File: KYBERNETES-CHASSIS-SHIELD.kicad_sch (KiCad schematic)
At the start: 42 parts, among them J1 ESC, J10 Fan, J2 Radio, J3 Encoder, J4 I2C, J5 Bumper, J6 Servo 1, J7 Servo 2, J8 Servo Regulator 1, J9 Servo Regulator 2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

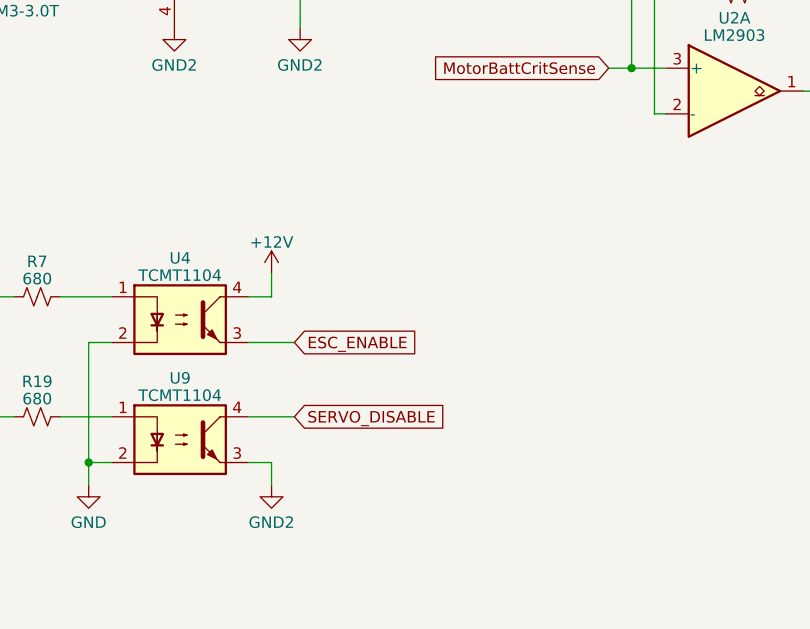
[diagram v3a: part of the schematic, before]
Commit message: add a mosfet after the esc enable opto to as it is not just an enable line as previously thought. needs more current than opto can provide.
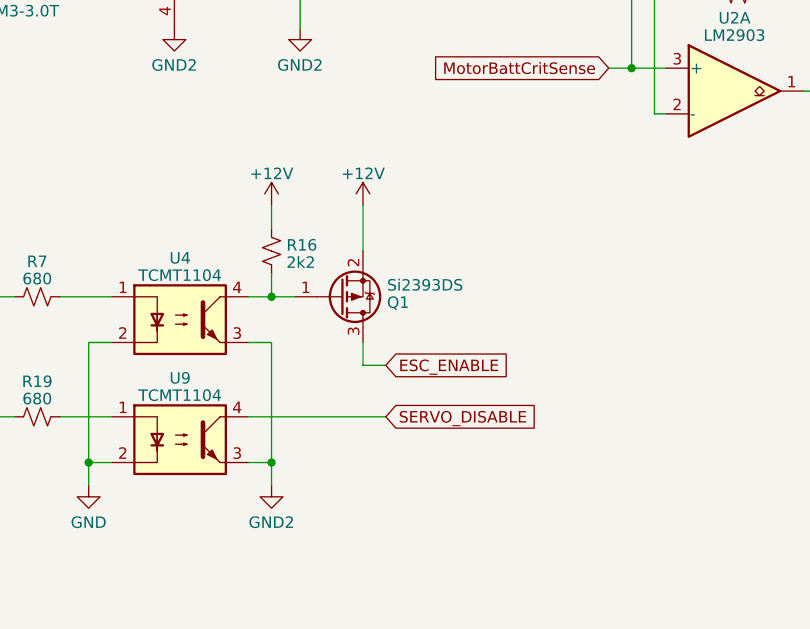
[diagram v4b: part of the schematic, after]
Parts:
- added Q1: Si2393DS, Package_TO_SOT_SMD:SOT-23, symbol Mosfets:Si2393DS
- added R16: 2k2, Resistor_SMD:R_0603_1608Metric_Pad0.98x0.95mm_HandSolder, symbol Device:R_Small_US
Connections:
- net +12V: now also Q1.2 (S), R16.1; no longer U4.4
- net ESC_ENABLE: now also Q1.3 (D); no longer U4.3
- net GND2: now also U4.3
- new net: Q1.1 (G), R16.2, U4.4
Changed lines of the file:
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@@
   (junction (at 116.84 250.19) (diameter 0) (color 0 0 0 0)
   )
+  (junction (at 137.795 175.895) (diameter 0) (color 0 0 0 0)
+  )
   (junction (at 117.475 59.055) (diameter 0) (color 0 0 0 0)
   )
@@
   (junction (at 145.415 236.855) (diameter 0) (color 0 0 0 0)
   )
+  (junction (at 137.795 194.31) (diameter 0) (color 0 0 0 0)
+  )
   (junction (at 297.18 64.135) (diameter 0) (color 0 0 0 0)
   )
@@
     (stroke (width 0) (type default))
   )
+  (wire (pts (xy 137.795 180.975) (xy 135.255 180.975))
+    (stroke (width 0) (type default))
+  )
   (wire (pts (xy 164.465 51.435) (xy 169.545 51.435))
     (stroke (width 0) (type default))
@@
     (stroke (width 0) (type default))
   )
+  (wire (pts (xy 147.955 183.515) (xy 150.495 183.515))
+    (stroke (width 0) (type default))
+  )
   (wire (pts (xy 40.005 136.525) (xy 40.005 137.795))
     (stroke (width 0) (type default))
@@
     (stroke (width 0) (type default))
   )
-  (wire (pts (xy 135.255 175.895) (xy 137.795 175.895))
-    (stroke (width 0) (type default))
-  )
   (wire (pts (xy 167.005 59.055) (xy 169.545 59.055))
     (stroke (width 0) (type default))
@@
     (stroke (width 0) (type default))
   )
-  (wire (pts (xy 137.795 173.355) (xy 137.795 175.895))
-    (stroke (width 0) (type default))
-  )
   (wire (pts (xy 145.415 236.855) (xy 155.575 236.855))
     (stroke (width 0) (type default))
@@
     (stroke (width 0) (type default))
   )
+  (wire (pts (xy 137.795 175.895) (xy 140.335 175.895))
+    (stroke (width 0) (type default))
+  )
   (wire (pts (xy 153.035 257.81) (xy 153.035 260.35))
     (stroke (width 0) (type default))
@@
     (stroke (width 0) (type default))
   )
-  (wire (pts (xy 135.255 189.23) (xy 140.335 189.23))
+  (wire (pts (xy 135.255 189.23) (xy 150.495 189.23))
     (stroke (width 0) (type default))
   )
@@
     (stroke (width 0) (type default))
   )
+  (wire (pts (xy 135.255 175.895) (xy 137.795 175.895))
+    (stroke (width 0) (type default))
+  )
   (wire (pts (xy 158.75 67.945) (xy 158.75 69.215))
     (stroke (width 0) (type default))
@@
     (stroke (width 0) (type default))
   )
+  (wire (pts (xy 147.955 165.735) (xy 147.955 170.815))
+    (stroke (width 0) (type default))
+  )
   (wire (pts (xy 117.475 59.055) (xy 117.475 69.215))
     (stroke (width 0) (type default))
@@
     (stroke (width 0) (type default))
   )
-  (wire (pts (xy 135.255 180.975) (xy 140.335 180.975))
-    (stroke (width 0) (type default))
-  )
   (wire (pts (xy 346.71 191.135) (xy 349.25 191.135))
     (stroke (width 0) (type default))
@@
     (stroke (width 0) (type default))
   )
+  (wire (pts (xy 137.795 165.735) (xy 137.795 168.275))
+    (stroke (width 0) (type default))
+  )
+  (wire (pts (xy 137.795 194.31) (xy 137.795 180.975))
+    (stroke (width 0) (type default))
+  )
+  (wire (pts (xy 147.955 180.975) (xy 147.955 183.515))
+    (stroke (width 0) (type default))
+  )
   (wire (pts (xy 342.9 147.955) (xy 346.71 147.955))
     (stroke (width 0) (type default))
@@
     (stroke (width 0) (type default))
   )
+  (wire (pts (xy 137.795 173.355) (xy 137.795 175.895))
+    (stroke (width 0) (type default))
+  )
   (wire (pts (xy 313.69 196.215) (xy 316.23 196.215))
     (stroke (width 0) (type default))
@@
     )
   )
-  (global_label "ESC_ENABLE" (shape input) (at 140.335 180.975 0) (fields_autoplaced)
+  (global_label "ESC_ENABLE" (shape input) (at 150.495 183.515 0) (fields_autoplaced)
     (effects (font (size 1.27 1.27)) (justify left))
-    (property "Intersheetrefs" "${INTERSHEET_REFS}" (at 154.8521 180.975 0)
+    (property "Intersheetrefs" "${INTERSHEET_REFS}" (at 165.0121 183.515 0)
       (effects (font (size 1.27 1.27)) (justify left) hide)
     )
@@
     )
   )
-  (global_label "SERVO_DISABLE" (shape input) (at 140.335 189.23 0) (fields_autoplaced)
+  (global_label "SERVO_DISABLE" (shape input) (at 150.495 189.23 0) (fields_autoplaced)
     (effects (font (size 1.27 1.27)) (justify left))
-    (property "Intersheetrefs" "${INTERSHEET_REFS}" (at 157.876 189.23 0)
+    (property "Intersheetrefs" "${INTERSHEET_REFS}" (at 168.036 189.23 0)
       (effects (font (size 1.27 1.27)) (justify left) hide)
     )
@@
     )
   )
+  (symbol (lib_id "Device:R_Small_US") (at 137.795 170.815 0) (unit 1)
+    (in_bom yes) (on_board yes) (dnp no) (fields_autoplaced)
+    (property "Reference" "R16" (at 139.446 170.1713 0)
+      (effects (font (size 1.27 1.27)) (justify left))
+    )
+    (property "Value" "2k2" (at 139.446 172.0923 0)
+      (effects (font (size 1.27 1.27)) (justify left))
+    )
+    (property "Footprint" "Resistor_SMD:R_0603_1608Metric_Pad0.98x0.95mm_HandSolder" (at 137.795 170.815 0)
+      (effects (font (size 1.27 1.27)) hide)
+    )
+    (property "Datasheet" "~" (at 137.795 170.815 0)
+      (effects (font (size 1.27 1.27)) hide)
+    )
+    (pin "1")
+    (pin "2")
+    (instances
+      (project "KYBERNETES-CHASSIS-SHIELD"
+        (path "/35172950-fd0b-46e4-875b-9133eac965de"
+          (reference "R16") (unit 1)
+        )
+      )
+      (project "KYBERNETES-CHASSIS-PD"
+        (path "/b9e34260-dded-46d4-944b-b6d38e23aefa"
+          (reference "R20") (unit 1)
+        )
+      )
+    )
+  )
   (symbol (lib_id "power:GND2") (at 117.475 69.215 0) (unit 1)
     (in_bom yes) (on_board yes) (dnp no) (fields_autoplaced)
@@
     )
   )
+  (symbol (lib_id "Mosfets:Si2393DS") (at 145.415 175.895 0) (mirror x) (unit 1)
+    (in_bom yes) (on_board yes) (dnp no)
+    (property "Reference" "Q1" (at 150.622 176.5387 0)
+      (effects (font (size 1.27 1.27)) (justify left))
+    )
+    (property "Value" "Si2393DS" (at 150.622 174.6177 0)
+      (effects (font (size 1.27 1.27)) (justify left))
+    )
+    (property "Footprint" "Package_TO_SOT_SMD:SOT-23" (at 150.495 173.99 0)
+      (effects (font (size 1.27 1.27) italic) (justify left) hide)
+    )
+    (property "Datasheet" "https://www.vishay.com/docs/70132/si2393ds.pdf" (at 145.415 175.895 0)
+      (effects (font (size 1.27 1.27)) (justify left) hide)
+    )
+    (pin "1")
+    (pin "2")
+    (pin "3")
+    (instances
+      (project "KYBERNETES-CHASSIS-SHIELD"
+        (path "/35172950-fd0b-46e4-875b-9133eac965de"
+          (reference "Q1") (unit 1)
+        )
+      )
+    )
+  )
   (symbol (lib_id "power:+12V") (at 40.005 128.905 0) (unit 1)
     (in_bom yes) (on_board yes) (dnp no) (fields_autoplaced)
@@
     )
   )
-  (symbol (lib_id "power:+12V") (at 137.795 173.355 0) (unit 1)
+  (symbol (lib_id "power:+12V") (at 137.795 165.735 0) (unit 1)
     (in_bom yes) (on_board yes) (dnp no) (fields_autoplaced)
-    (property "Reference" "#PWR029" (at 137.795 177.165 0)
+    (property "Reference" "#PWR029" (at 137.795 169.545 0)
       (effects (font (size 1.27 1.27)) hide)
     )
-    (property "Value" "+12V" (at 137.795 169.8531 0)
+    (property "Value" "+12V" (at 137.795 162.2331 0)
       (effects (font (size 1.27 1.27)))
     )
-    (property "Footprint" "" (at 137.795 173.355 0)
+    (property "Footprint" "" (at 137.795 165.735 0)
       (effects (font (size 1.27 1.27)) hide)
     )
-    (property "Datasheet" "" (at 137.795 173.355 0)
+    (property "Datasheet" "" (at 137.795 165.735 0)
       (effects (font (size 1.27 1.27)) hide)
     )
@@
         )
       )
+    )
+  )
+  (symbol (lib_id "power:+12V") (at 147.955 165.735 0) (unit 1)
+    (in_bom yes) (on_board yes) (dnp no) (fields_autoplaced)
+    (property "Reference" "#PWR052" (at 147.955 169.545 0)
+      (effects (font (size 1.27 1.27)) hide)
+    )
+    (property "Value" "+12V" (at 147.955 162.2331 0)
+      (effects (font (size 1.27 1.27)))
+    )
+    (property "Footprint" "" (at 147.955 165.735 0)
+      (effects (font (size 1.27 1.27)) hide)
+    )
+    (property "Datasheet" "" (at 147.955 165.735 0)
+      (effects (font (size 1.27 1.27)) hide)
+    )
+    (pin "1")
+    (instances
+      (project "KYBERNETES-CHASSIS-SHIELD"
+        (path "/35172950-fd0b-46e4-875b-9133eac965de"
+          (reference "#PWR052") (unit 1)
+        )
+      )

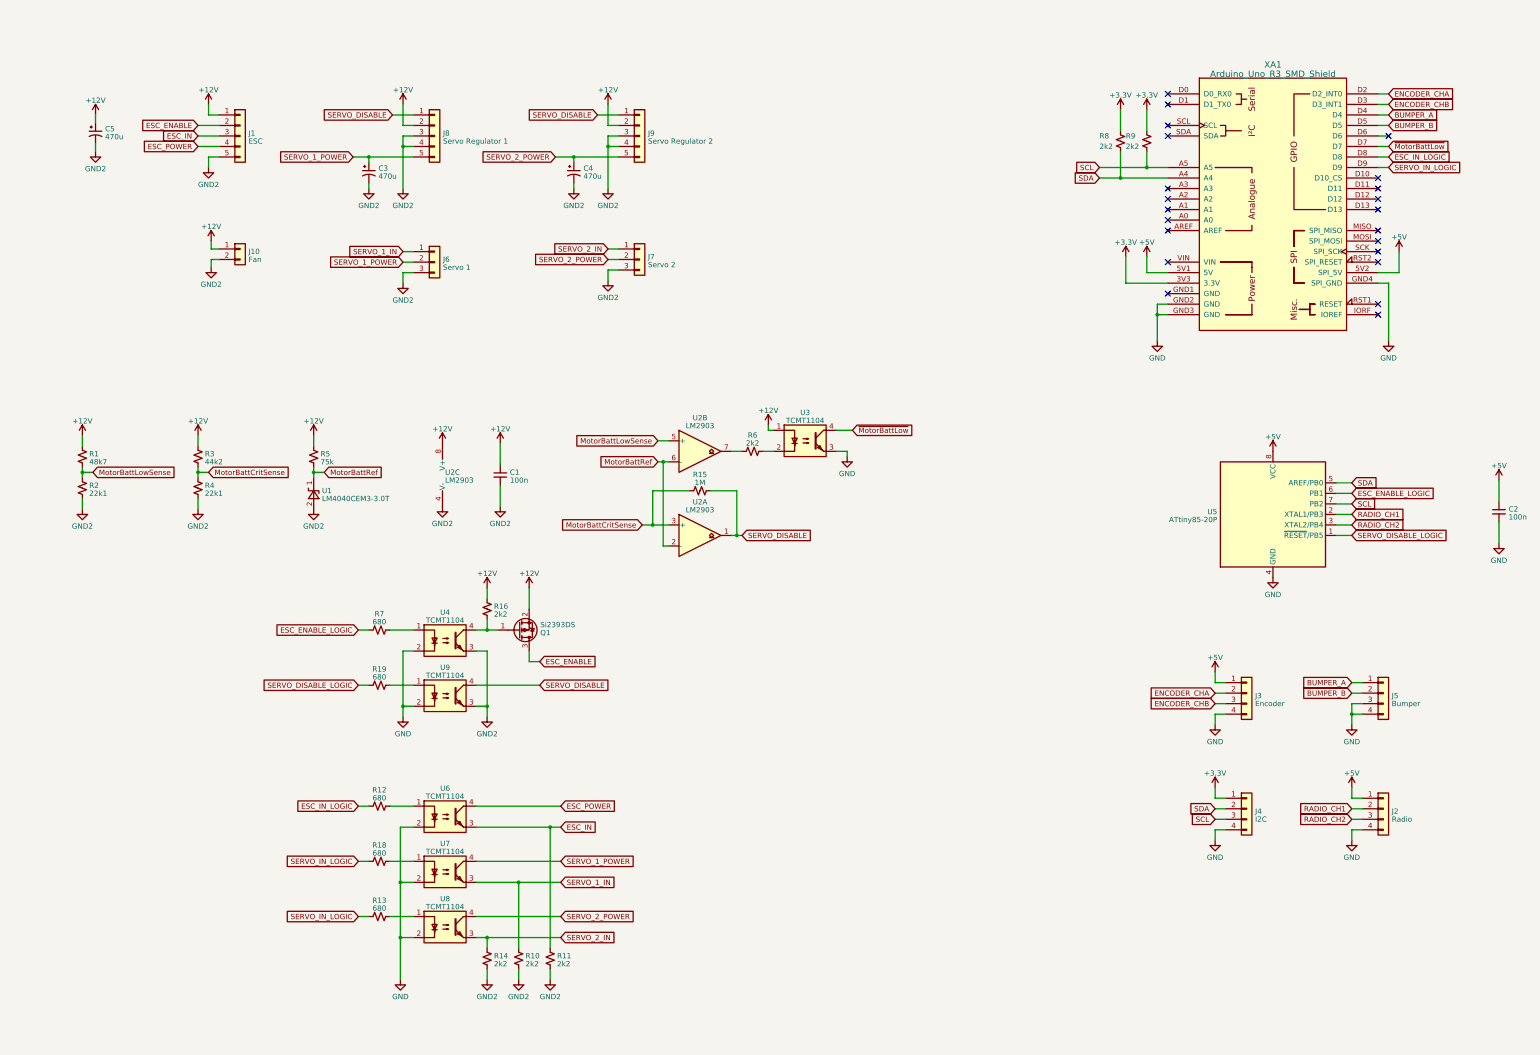
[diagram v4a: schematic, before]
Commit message: change the servo enable optoisolator to a high side switch
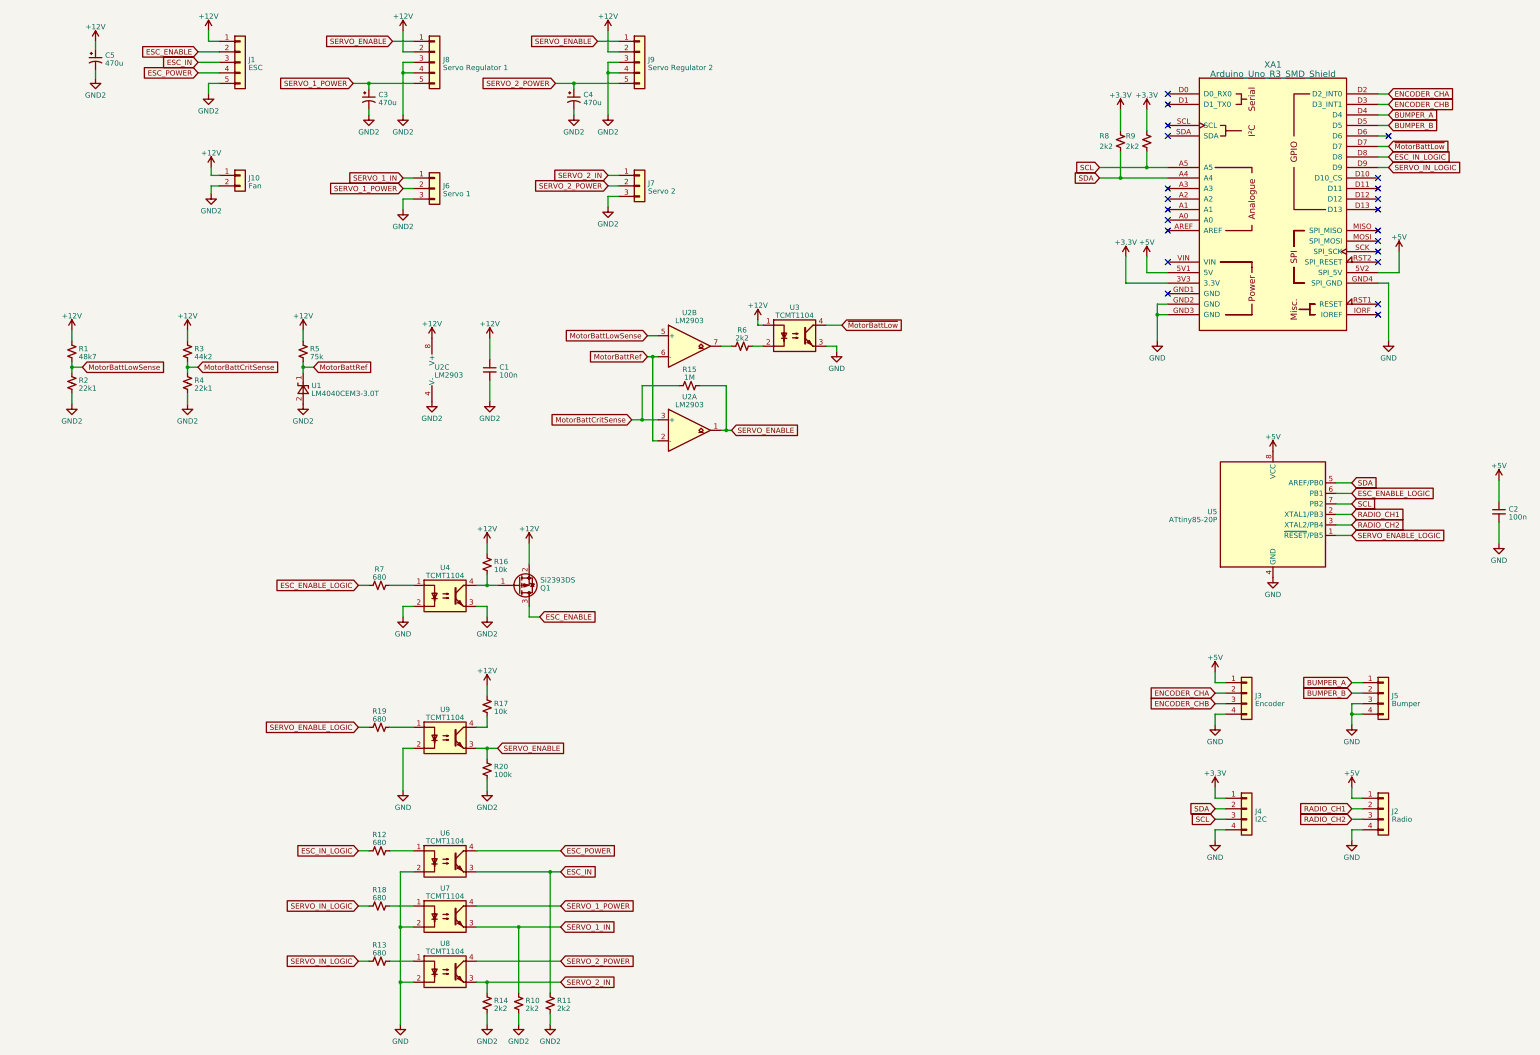
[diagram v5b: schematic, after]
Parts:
- added R17: 10k, Resistor_SMD:R_0603_1608Metric_Pad0.98x0.95mm_HandSolder, symbol Device:R_Small_US
- added R20: 100k, Resistor_SMD:R_0603_1608Metric_Pad0.98x0.95mm_HandSolder, symbol Device:R_Small_US
- R16: value 2k2 -> 10k
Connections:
- net +12V: now also R17.1
- net GND2: now also R20.2; no longer U9.3
- net SERVO_DISABLE renamed SERVO_ENABLE
- net SERVO_ENABLE: now also U9.3, R20.1; no longer U9.4
- net SERVO_DISABLE_LOGIC renamed SERVO_ENABLE_LOGIC
- new net: R17.2, U9.4
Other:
- moved on the sheet: C1, C3, C4, C5, J1, J10, J6, J7, J8, J9, Q1, R1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
